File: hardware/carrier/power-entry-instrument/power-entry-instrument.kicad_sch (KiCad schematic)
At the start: 15 parts

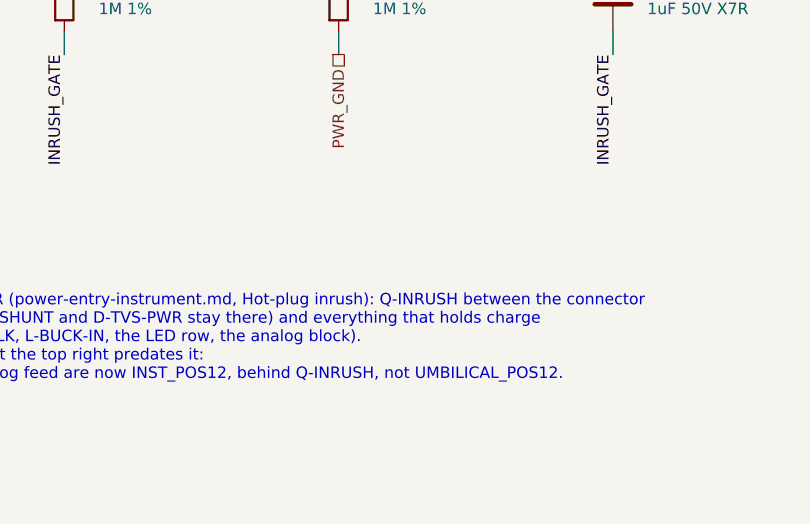
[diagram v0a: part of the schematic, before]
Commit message: Owner decisions D1, D2, D3, D5, CMRR: the parts on the sheets (#11, #14, #15, #16, #5, #12)
The owner's choices of 2026-10-03 (working chat), applied to the KiCad sheets,
exported, rendered, and carried into the BOM fragments:

- D1 (#11 F2, #14 A1, #12-3), "10 ohm + 22 uF + 10 uF": breath-adc gains
  R-ADC-VDD (10R 1% 0805, UNI-ROYAL 0805W8F100JT5E, C17415, JLC basic) from
  DEV_3V3 to a new local net ADC_VDD = U-ADC pin 8, with C-ADC-VDD (22 uF
  X5R 25 V 1206, Samsung CL31A226KAHNNNE, C12891, JLC basic) beside the
  existing C-ADC-BULK and C-DEC-ADC (C3 kept); a PWR_FLAG on ADC_VDD for
  ERC. power-entry-instrument gains C-BUCK-OUT (10 uF X5R 50 V 1206,
  Samsung CL31A106KBHNNNE, C13585, JLC basic) at U-BUCK-A's OUT (main-board
  U5, the R-78E5.0 - RECOM's standard application, #14 A1 item 3).
  Main board: R47, C42, C43.
- D5: U-ADC CH1 tied to AGND_INST.
- D2 (#15 C2, #16 B2), "Yes, all 4 channels": a second SP0504BAHTG at J5
  on CHAIN_SCK, CHAIN_SHLD, HOP_LT_RH, HOP_RH_RT - main-board U11 on the
  root sheet, U-TVS-CHAIN-RH on the key-chain-loom sheet; row qty 2.
- D3 (#15 C3): R-SPI-SER (R1-R3) Panasonic ERJ-P08F82R0V (C4065013, 0 at
  JLC and LCSC; in-stock equivalent Vishay CRCW120682R0FKEAHP, C1854869,
  named in the row); R-SER-BREATH-INST (R38/R39) ERJ-P08F1001V (C4261071,
  JLC 4,299).
- CMRR (#5-5), "Tighten cap matching": C-CM-BREATH a matched pair, each
  within 0.5 % of the pair's mean, from one reel of the 1 % C0G, measured
  and hand-fitted (no 1.5 nF C0G is catalogued tighter than 1 %).

Banked: Samsung CL31A226KAHNNNE and CL31A106KBHNNNE spec sheets, Vishay
CRCW-HP e3 (fragment .manifest-R51-owner-decisions.csv). Also two module
sims the deff676 merge staled and these changes do not touch (panel-led,
digital-and-supervision) re-run: 0 failed.

Gate-Red: sims staled by these netlists are re-running in the next commits; main-board .kicad_pcb awaits wave-3 placement of R47, C42, C43, U11 (and fab/ renders); known stale photos/clash

Co-Authored-By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
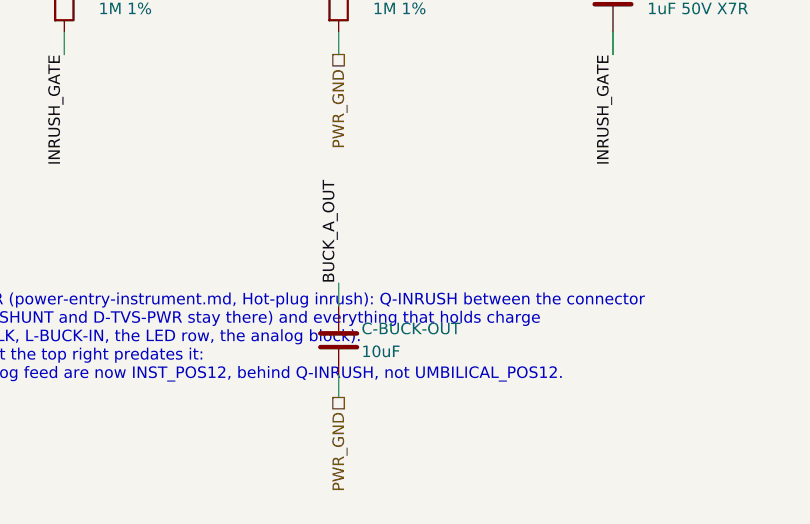
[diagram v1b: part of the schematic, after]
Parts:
- added C-BUCK-OUT: 10uF, Capacitor_SMD:C_1206_3216Metric, symbol Device:C
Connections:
- net BUCK_A_OUT: now also C-BUCK-OUT.1
- net PWR_GND: now also C-BUCK-OUT.2
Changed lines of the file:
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@@
     (property "Figure" "umbilical-pinmap" (at 255.27 142.24 0) (effects (font (size 1.27 1.27)) hide)))
   (text "HOT-PLUG INRUSH LIMITER (power-entry-instrument.md, Hot-plug inrush): Q-INRUSH between the connector\n(UMBILICAL_POS12, D-REVSHUNT and D-TVS-PWR stay there) and everything that holds charge\n (INST_POS12: C-STRIP-BULK, L-BUCK-IN, the LED row, the analog block).\nThe verbatim netlist text at the top right predates it:\nthe strip feed and the analog feed are now INST_POS12, behind Q-INRUSH, not UMBILICAL_POS12." (at 40.64 175.26 0) (effects (font (size 1.27 1.27)) (justify left top)))
+  (symbol (lib_id "Device:C") (at 101.6 180.34 0) (unit 1)
+    (in_bom yes) (on_board yes) (dnp no)
+    (property "Reference" "C-BUCK-OUT" (at 104.14 179.07 0) (effects (font (size 1.27 1.27)) (justify left)))
+    (property "Value" "10uF" (at 104.14 181.61 0) (effects (font (size 1.27 1.27)) (justify left)))
+    (property "Footprint" "Capacitor_SMD:C_1206_3216Metric" (at 101.60 180.34 0) (effects (font (size 1.27 1.27)) hide))
+    (property "Datasheet" "" (at 101.60 180.34 0) (effects (font (size 1.27 1.27)) hide))
+    (property "Row" "C-BUCK-OUT" (at 101.60 180.34 0) (effects (font (size 1.27 1.27)) hide))
+    (property "Pins" "1=1 2=2" (at 101.60 180.34 0) (effects (font (size 1.27 1.27)) hide))
+    (property "Note" "D1 (owner, 2026-10-03: '10 ohm + 22 uF + 10 uF'): RECOM's standard-application output capacitor, a 10 uF MLCC at U-BUCK-A's OUT pin (R-78E5.0-1.0 datasheet p.I-4), returned to its GND pin. It lowers the converter's ripple at its source, ahead of D-USBOR-A. Well inside the part's 220 uF capacitive-load limit" (at 101.60 180.34 0) (effects (font (size 1.27 1.27)) hide))
+    (property "Pins_source" "a two-terminal capacitor" (at 101.60 180.34 0) (effects (font (size 1.27 1.27)) hide))
+    (property "Manufacturer" "Samsung Electro-Mechanics" (at 101.60 180.34 0) (effects (font (size 1.27 1.27)) hide))
+    (property "MPN" "CL31A106KBHNNNE" (at 101.60 180.34 0) (effects (font (size 1.27 1.27)) hide))
+    (property "LCSC" "C13585" (at 101.60 180.34 0) (effects (font (size 1.27 1.27)) hide))
+    (property "Assembly" "machine" (at 101.60 180.34 0) (effects (font (size 1.27 1.27)) hide))
+    (pin "1")
+    (pin "2")
+    (instances (project "main-board" (path "/b12a49ac-ffa0-5078-b2ba-e15d161f1936/4727eca5-0a6b-5761-98ac-51ca9f544ea2" (reference "C43") (unit 1))) (project "power-entry-instrument" (path "/ba12e546-d582-5654-bb26-6a94a8f78514" (reference "C-BUCK-OUT") (unit 1))))
+  )
+  (wire (pts (xy 101.6 176.53) (xy 101.6 173.99)) (stroke (width 0) (type default)))
+  (label "BUCK_A_OUT" (at 101.6 173.99 90) (fields_autoplaced) (effects (font (size 1.27 1.27)) (justify left bottom)))
+  (wire (pts (xy 101.6 184.15) (xy 101.6 186.69)) (stroke (width 0) (type default)))
+  (hierarchical_label "PWR_GND" (shape passive) (at 101.6 186.69 270) (effects (font (size 1.27 1.27)) (justify right))
+    (property "Dir" "ref" (at 101.6 186.69 0) (effects (font (size 1.27 1.27)) hide))
+    (property "From" "module/power-entry" (at 101.6 186.69 0) (effects (font (size 1.27 1.27)) hide))
+    (property "Figure" "umbilical-pinmap" (at 101.6 186.69 0) (effects (font (size 1.27 1.27)) hide)))
   (sheet_instances (path "/" (page "1")))
 )

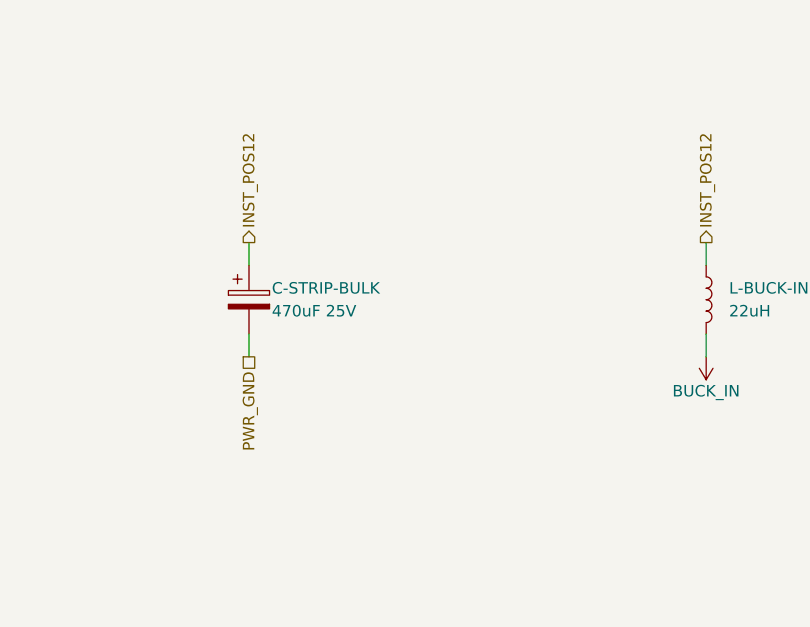
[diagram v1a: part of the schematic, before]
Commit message: #19 #8: thirteen LEDs (tail-end LED removed, owner); C-STRIP-BULK two 6.3x7.7 polymer cans; J-MCU at 262.27
The owner, 2026-10-03: "remove that bottom led again" / "Keep current
layout, remove bottom one". ADR 0028 second amendment of 2026-10-03.

- lighting.led_count 14 -> 13; new lighting.led_slots 14 keeps LED2-14
  where they stood (pitch 19.869, x 24.55 ... 262.98), now LED1-13;
  drc.echo 'LED row on the main board' prints count and places.
- led-strip-drive sheet: D-LED-1 / C-LED-1 (D7 / C25) removed, the chain
  renumbered from the tail with every part's UUID kept; new D-LED-1's DIN2
  grounded; BOM qty 13.
- Figures by the three-step rule (the 14-LED spellings grepped first, moved
  into forbidden; the 13-LED spellings that are correct again taken out):
  led-row-current 170-195 mA, umbilical-current 359 mA, hotplug-iso-ocp
  0.49-0.54 A / 3.4x, instrument-input-z-margin 55x / 159x, led-pwm-rail-ripple
  5.6 mV / 0.00088 cents, led-pwm-pitch 0.0034 / 0.011 cents,
  diode-split-rationale back at 0.22 A.
- C10 replacement (coordinator-approved, all four criteria hold):
  C-STRIP-BULK is two MA25V220M6X8 (JIERR, LCSC C46550464), 220 uF 25 V
  polymer, 6.3 x 7.7 mm, in parallel (C10, C44): 14 mohm at 100 kHz
  (<= 0.16), ripple 2.9 A x 0.3 at 1-10 kHz per can vs a 0.367 A swing,
  440 uF; every sim that takes the bulk now takes the pair (c_strip,
  r_strip) and passes. Datasheet and EasyEDA footprint banked (fragment
  R52), JLC rotation row by pin function (0).
- Sims re-run, not scaled, 0 failed: led-strip-drive, power-entry-instrument,
  umbilical-load-switch, panel-led, digital-and-supervision, power-entry,
  interfaces/system, breath-adc, breath-output-stage.
- ADR 0005, 0014, 0016, 0021, 0027, 0028 (amendment), firmware README
  (13 pixels), led-strip-drive, power-entry-instrument, power-entry,
  umbilical-load-switch pages and sim READMEs follow.
- boards.mcu_conn_at [262.27, 12.29, 90] (the owner's option 1; the
  Matrix branch carries the same line); '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
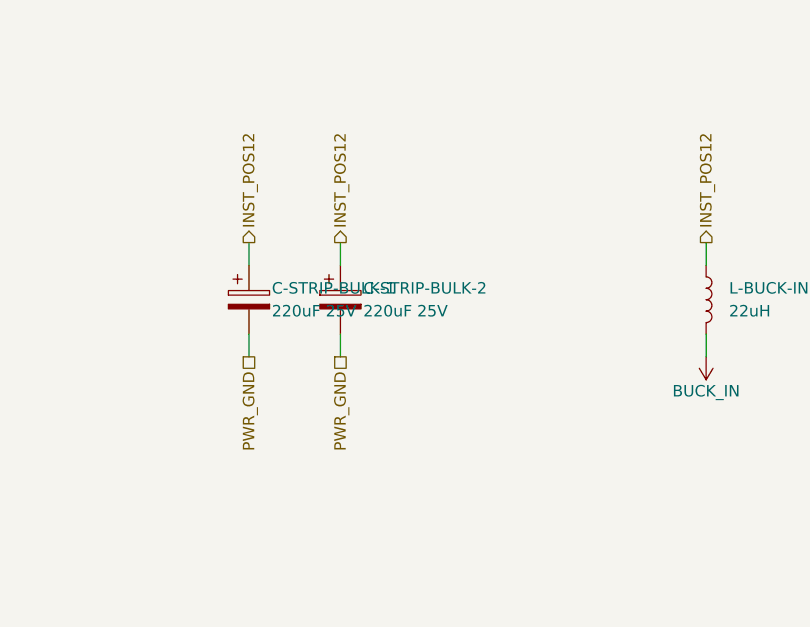
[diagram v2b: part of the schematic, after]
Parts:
- added C-STRIP-BULK-2: 220uF 25V, Capacitor_SMD:CP_Elec_6.3x7.7, symbol Device:C_Polarized
- C-STRIP-BULK-1: renamed from C-STRIP-BULK; value 470uF 25V -> 220uF 25V; footprint Capacitor_SMD:CP_Elec_10x10 -> Capacitor_SMD:CP_Elec_6.3x7.7; LCSC C340751 -> C46550464; MPN UCW1E471MNL1GS -> MA25V220M6X8; Manufacturer Nichicon -> JIERR; Note At the LED row's 12 V feed end. Bulk belongs where the curr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 -> At the LED row's 12 V feed end, ONE OF TWO IN PARALLEL: bul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
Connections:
- net INST_POS12: now also C-STRIP-BULK-2.1
- net PWR_GND: now also C-STRIP-BULK-2.2
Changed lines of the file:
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@@
   (symbol (lib_id "Device:C_Polarized") (at 142.24 50.8 0) (unit 1)
     (in_bom yes) (on_board yes) (dnp no)
-    (property "Reference" "C-STRIP-BULK" (at 144.78 49.53 0) (effects (font (size 1.27 1.27)) (justify left)))
-    (property "Value" "470uF 25V" (at 144.78 52.07 0) (effects (font (size 1.27 1.27)) (justify left)))
-    (property "Footprint" "Capacitor_SMD:CP_Elec_10x10" (at 143.51 54.61 0) (effects (font (size 1.27 1.27)) hide))
+    (property "Reference" "C-STRIP-BULK-1" (at 144.78 49.53 0) (effects (font (size 1.27 1.27)) (justify left)))
+    (property "Value" "220uF 25V" (at 144.78 52.07 0) (effects (font (size 1.27 1.27)) (justify left)))
+    (property "Footprint" "Capacitor_SMD:CP_Elec_6.3x7.7" (at 143.51 54.61 0) (effects (font (size 1.27 1.27)) hide))
     (property "Datasheet" "" (at 142.24 50.8 0) (effects (font (size 1.27 1.27)) hide))
     (property "Row" "C-STRIP-BULK" (at 142.24 50.8 0) (effects (font (size 1.27 1.27)) hide))
     (property "Pins" "1=1 2=2" (at 142.24 50.8 0) (effects (font (size 1.27 1.27)) hide))
-    (property "Note" "At the LED row's 12 V feed end. Bulk belongs where the current swings: the row's PWM steps its whole current at once, and each LED's own 100 nF (C-LED) takes only the edges (ADR 0028)" (at 142.24 50.8 0) (effects (font (size 1.27 1.27)) hide))
+    (property "Note" "At the LED row's 12 V feed end, ONE OF TWO IN PARALLEL: bulk belongs where the current swings: the row's PWM steps its whole current at once, and each LED's own 100 nF (C-LED) takes only the edges (ADR 0028). Two 6.3 x 7.7 polymer cans, not one 10 x 10 electrolytic, so the bulk stands 7.7 mm, not 10.2, in the LEDs' cone (#19): 440 uF and 14 mohm together [ds JIERR-MA-SERIES-MA25V220M6X8.pdf p.3]" (at 142.24 50.8 0) (effects (font (size 1.27 1.27)) hide))
     (property "Pins_source" "pin 1 is the positive terminal" (at 142.24 50.8 0) (effects (font (size 1.27 1.27)) hide))
-    (property "Manufacturer" "Nichicon" (at 142.24 50.8 0) (effects (font (size 1.27 1.27)) hide))
-    (property "MPN" "UCW1E471MNL1GS" (at 142.24 50.8 0) (effects (font (size 1.27 1.27)) hide))
-    (property "LCSC" "C340751" (at 142.24 50.8 0) (effects (font (size 1.27 1.27)) hide))
+    (property "Manufacturer" "JIERR" (at 142.24 50.8 0) (effects (font (size 1.27 1.27)) hide))
+    (property "MPN" "MA25V220M6X8" (at 142.24 50.8 0) (effects (font (size 1.27 1.27)) hide))
+    (property "LCSC" "C46550464" (at 142.24 50.8 0) (effects (font (size 1.27 1.27)) hide))
     (property "Assembly" "machine" (at 142.24 50.8 0) (effects (font (size 1.27 1.27)) hide))
     (pin "1")
     (pin "2")
-    (instances (project "main-board" (path "/b12a49ac-ffa0-5078-b2ba-e15d161f1936/4727eca5-0a6b-5761-98ac-51ca9f544ea2" (reference "C10") (unit 1))) (project "power-entry-instrument" (path "/ba12e546-d582-5654-bb26-6a94a8f78514" (reference "C-STRIP-BULK") (unit 1))))
+    (instances (project "main-board" (path "/b12a49ac-ffa0-5078-b2ba-e15d161f1936/4727eca5-0a6b-5761-98ac-51ca9f544ea2" (reference "C10") (unit 1))) (project "power-entry-instrument" (path "/ba12e546-d582-5654-bb26-6a94a8f78514" (reference "C-STRIP-BULK-1") (unit 1))))
+  )  (symbol (lib_id "Device:C_Polarized") (at 152.4 50.8 0) (unit 1)
+    (in_bom yes) (on_board yes) (dnp no)
+    (property "Reference" "C-STRIP-BULK-2" (at 154.94 49.53 0) (effects (font (size 1.27 1.27)) (justify left)))
+    (property "Value" "220uF 25V" (at 154.94 52.07 0) (effects (font (size 1.27 1.27)) (justify left)))
+    (property "Footprint" "Capacitor_SMD:CP_Elec_6.3x7.7" (at 153.67 54.61 0) (effects (font (size 1.27 1.27)) hide))
+    (property "Datasheet" "" (at 152.4 50.8 0) (effects (font (size 1.27 1.27)) hide))
+    (property "Row" "C-STRIP-BULK" (at 152.4 50.8 0) (effects (font (size 1.27 1.27)) hide))
+    (property "Pins" "1=1 2=2" (at 152.4 50.8 0) (effects (font (size 1.27 1.27)) hide))
+    (property "Note" "At the LED row's 12 V feed end, ONE OF TWO IN PARALLEL: bulk belongs where the current swings: the row's PWM steps its whole current at once, and each LED's own 100 nF (C-LED) takes only the edges (ADR 0028). Two 6.3 x 7.7 polymer cans, not one 10 x 10 electrolytic, so the bulk stands 7.7 mm, not 10.2, in the LEDs' cone (#19): 440 uF and 14 mohm together [ds JIERR-MA-SERIES-MA25V220M6X8.pdf p.3]" (at 152.4 50.8 0) (effects (font (size 1.27 1.27)) hide))
+    (property "Pins_source" "pin 1 is the positive terminal" (at 152.4 50.8 0) (effects (font (size 1.27 1.27)) hide))
+    (property "Manufacturer" "JIERR" (at 152.4 50.8 0) (effects (font (size 1.27 1.27)) hide))
+    (property "MPN" "MA25V220M6X8" (at 152.4 50.8 0) (effects (font (size 1.27 1.27)) hide))
+    (property "LCSC" "C46550464" (at 152.4 50.8 0) (effects (font (size 1.27 1.27)) hide))
+    (property "Assembly" "machine" (at 152.4 50.8 0) (effects (font (size 1.27 1.27)) hide))
+    (pin "1")
+    (pin "2")
+    (instances (project "main-board" (path "/b12a49ac-ffa0-5078-b2ba-e15d161f1936/4727eca5-0a6b-5761-98ac-51ca9f544ea2" (reference "C44") (unit 1))) (project "power-entry-instrument" (path "/ba12e546-d582-5654-bb26-6a94a8f78514" (reference "C-STRIP-BULK-2") (unit 1))))
   )
   (symbol (lib_id "Device:L") (at 193.04 50.8 0) (unit 1)
@@
     (property "From" "module/umbilical-load-switch" (at 85.09 50.8 0) (effects (font (size 1.27 1.27)) hide))
     (property "Figure" "umbilical-current" (at 85.09 50.8 0) (effects (font (size 1.27 1.27)) hide)))
+  (wire (pts (xy 152.4 46.99) (xy 152.4 44.45)) (stroke (width 0) (type default)))
+  (wire (pts (xy 152.4 54.61) (xy 152.4 57.15)) (stroke (width 0) (type default)))
+  (hierarchical_label "INST_POS12" (shape output) (at 152.4 44.45 90) (effects (font (size 1.27 1.27)) (justify left))
+    (property "Dir" "out" (at 152.4 44.45 0) (effects (font (size 1.27 1.27)) hide))
+    (property "To" "carrier/led-strip-drive" (at 152.4 44.45 0) (effects (font (size 1.27 1.27)) hide))
+    (property "Figure" "umbilical-current" (at 152.4 44.45 0) (effects (font (size 1.27 1.27)) hide)))
+  (hierarchical_label "PWR_GND" (shape passive) (at 152.4 57.15 270) (effects (font (size 1.27 1.27)) (justify right))
+    (property "Dir" "ref" (at 152.4 57.15 0) (effects (font (size 1.27 1.27)) hide))
+    (property "From" "module/power-entry" (at 152.4 57.15 0) (effects (font (size 1.27 1.27)) hide))
+    (property "Figure" "umbilical-pinmap" (at 152.4 57.15 0) (effects (font (size 1.27 1.27)) hide)))
   (wire (pts (xy 142.24 46.99) (xy 142.24 44.45)) (stroke (width 0) (type default)))
   (hierarchical_label "INST_POS12" (shape output) (at 142.24 44.45 90) (effects (font (size 1.27 1.27)) (justify left))
